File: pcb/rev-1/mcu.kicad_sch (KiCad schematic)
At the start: 8 parts, among them J4 BD125-10-A-0305-0580-L-B, U6 WT02C40C-V3

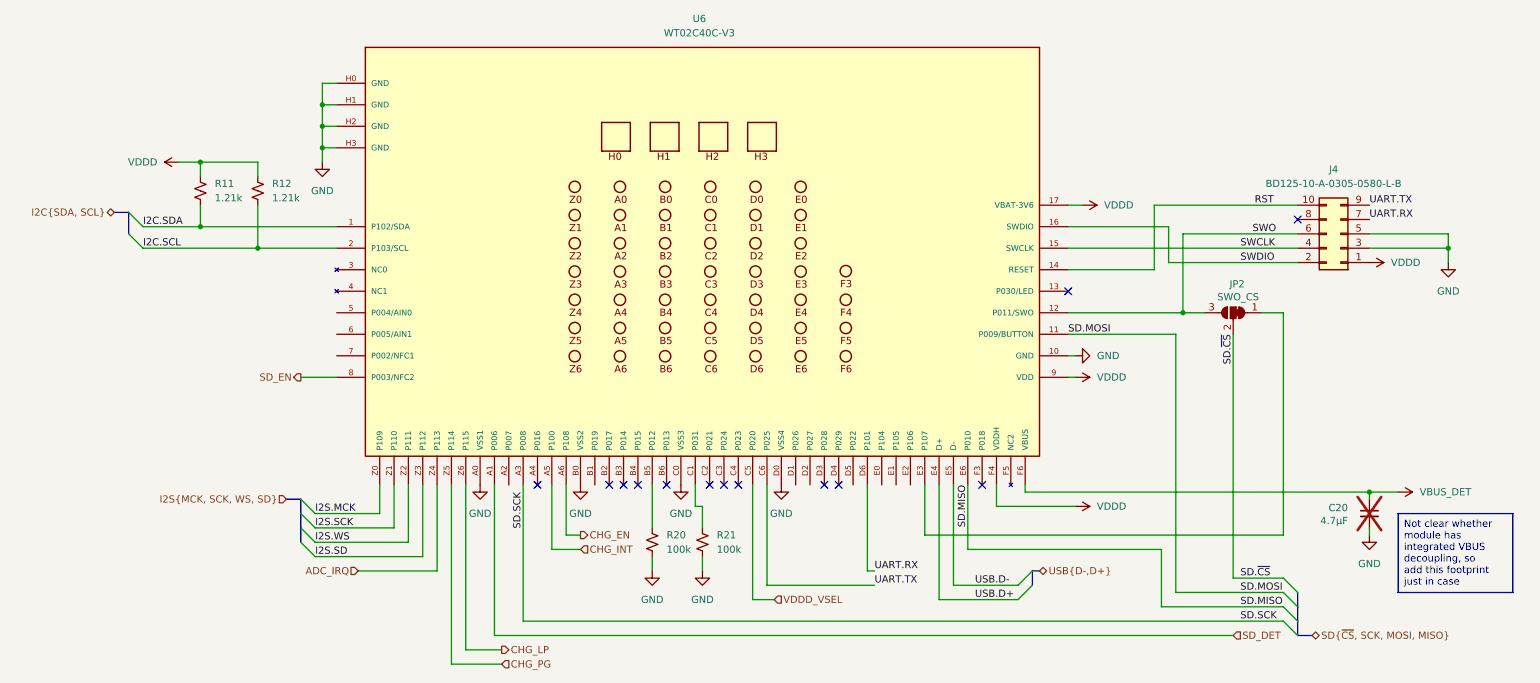
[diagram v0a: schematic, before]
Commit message: Update PCBs
* Update to KiCad 10
* Update footprint for nRF53 module based on 1.01 datasheet with
  actually readable mechanical drawing
* Add 3D model for production nRF53 module
* Remove overlapping silkscreen on rev-1 with production nRF53 module
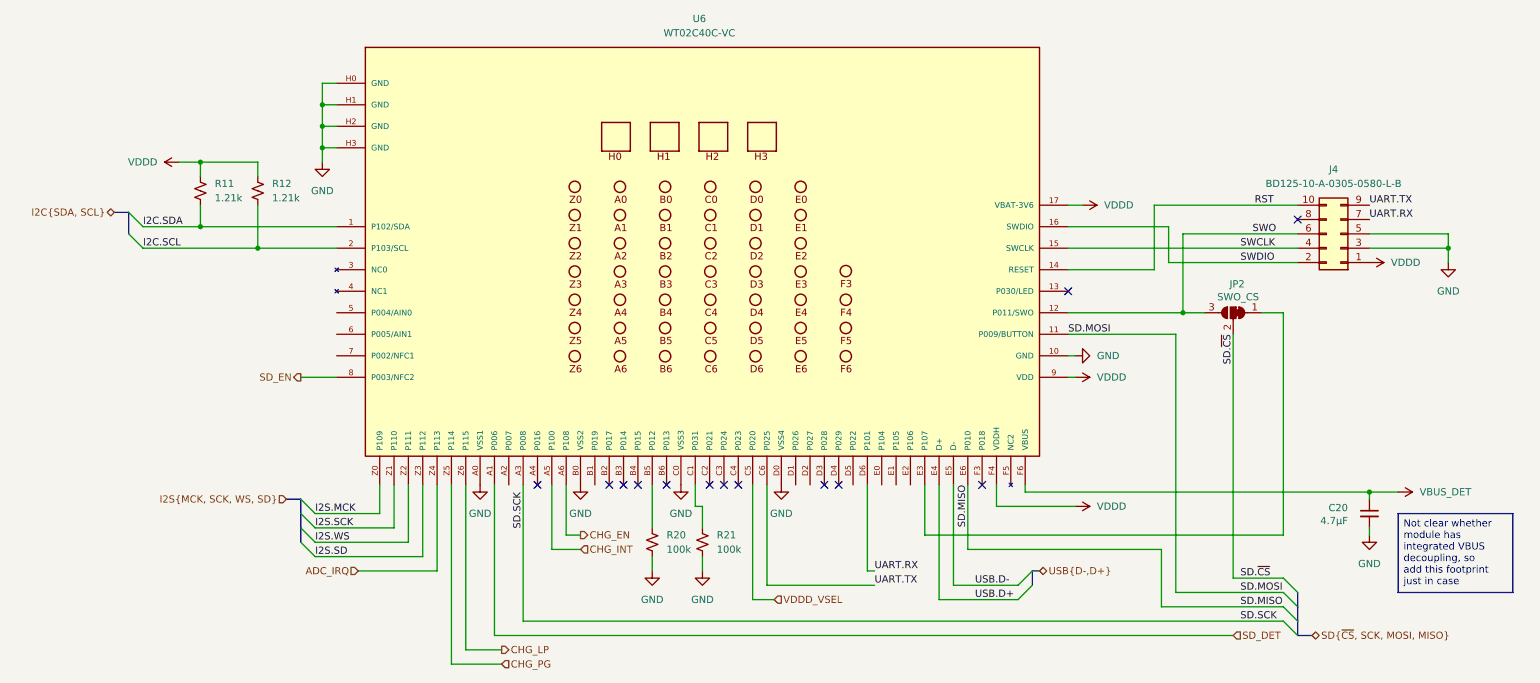
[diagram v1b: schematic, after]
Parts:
- C20: now fitted
- U6: value WT02C40C-V3 -> WT02C40C-VC; footprint zeus-le:WT02C40C -> zeus-le:WT02C40C-VC; symbol zeus-le:WT02V40V -> zeus-le:WT02C40C
